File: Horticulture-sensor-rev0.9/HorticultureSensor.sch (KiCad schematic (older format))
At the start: 23 parts, among them J1 Conn_01x04, J2 Conn_02x05_Odd_Even, J3 Conn_01x03, J4 Conn_01x04, J5 Conn_01x03, J6 Conn_01x02, J7 Conn_01x02, J8 Conn_01x01_MountingPin, J9 Conn_01x01_MountingPin, Q1 IRLML2030TRPBF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

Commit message: Initial sensor design
Almost finished, need to work out how power connection should work.
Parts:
- J4: footprint Connector_Molex:Molex_PicoBlade_53398-0371_1x03-1MP_P1.25mm_Vertical -> Connector_Molex:Molex_PicoBlade_53261-0371_1x03-1MP_P1.25mm_Horizontal
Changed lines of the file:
@@
 F 0 "J4" H 11780 6642 50  0000 L CNN
 F 1 "Conn_01x04" H 11780 6551 50  0000 L CNN
-F 2 "Connector_Molex:Molex_PicoBlade_53398-0371_1x03-1MP_P1.25mm_Vertical" H 11700 6650 50  0001 C CNN
+F 2 "Connector_Molex:Molex_PicoBlade_53261-0371_1x03-1MP_P1.25mm_Horizontal" H 11700 6650 50  0001 C CNN
 F 3 "~" H 11700 6650 50  0001 C CNN
 	1    11700 6650

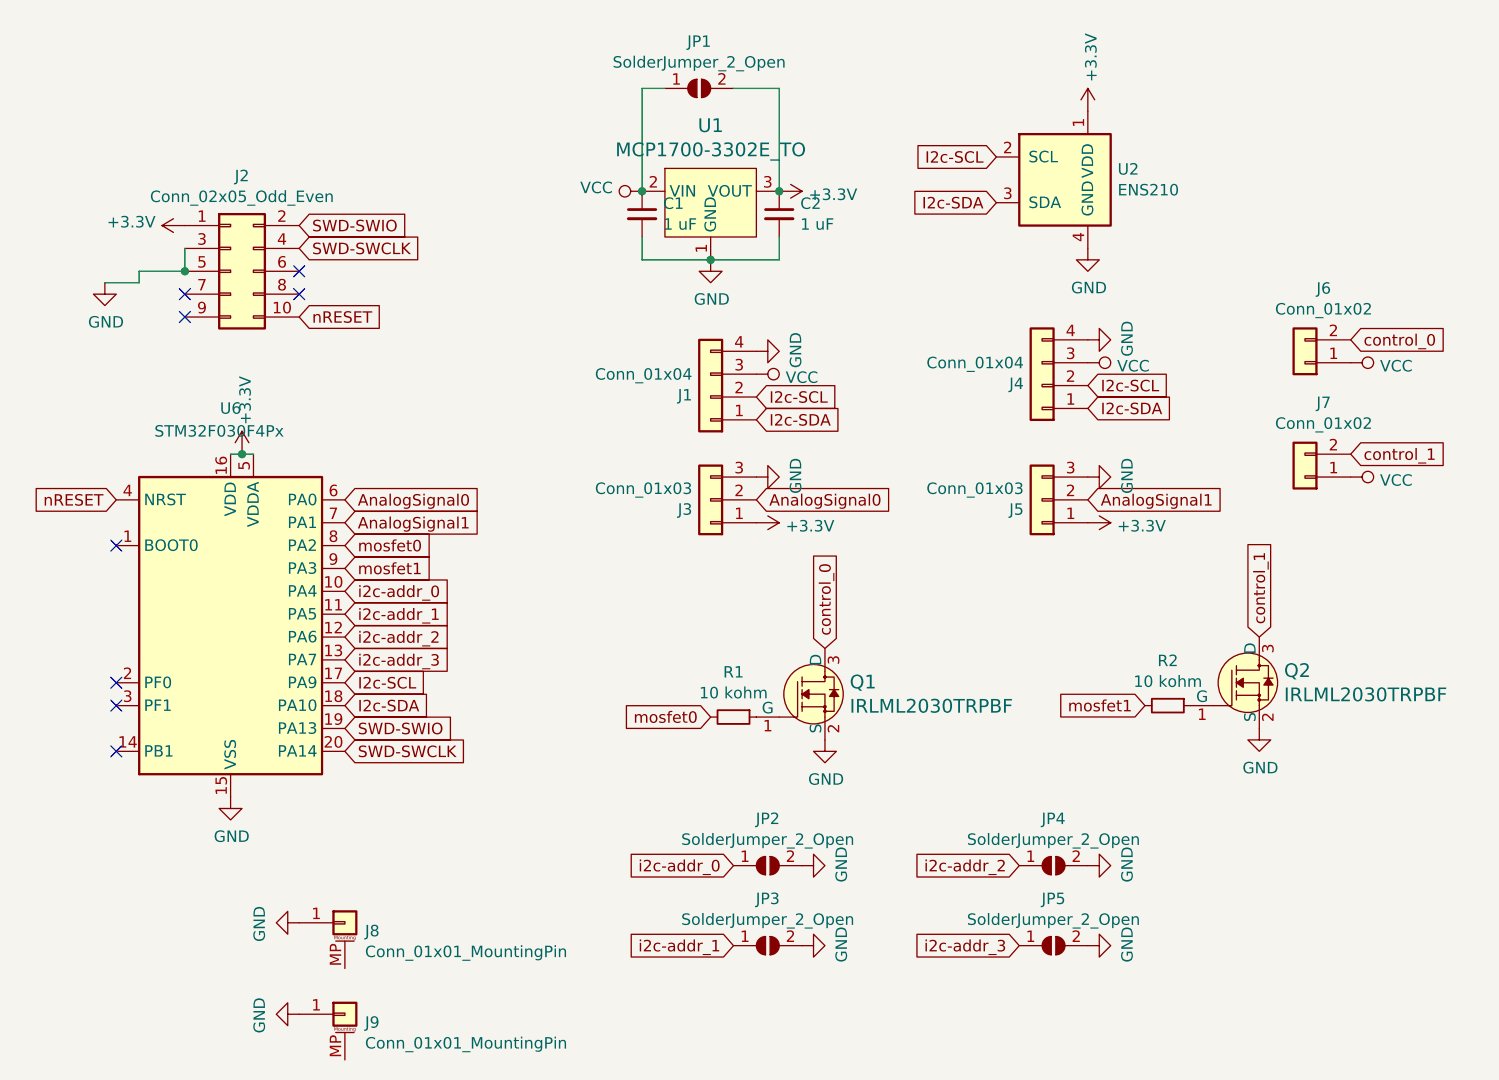
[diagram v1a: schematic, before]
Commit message: Working on sensor board
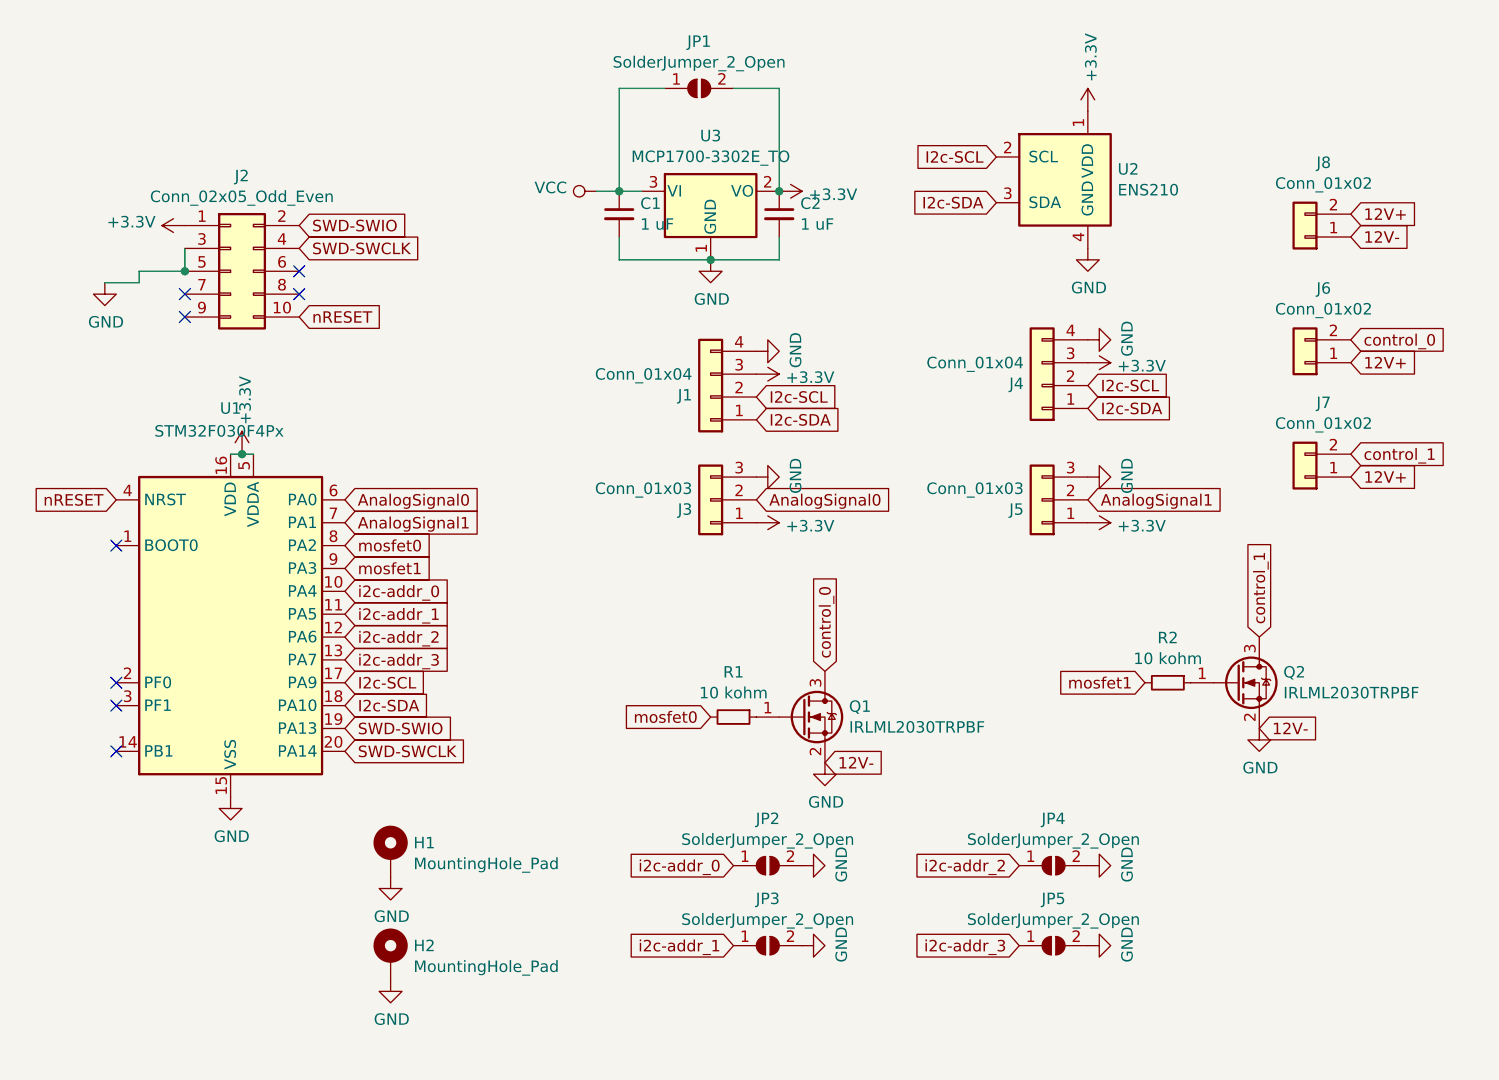
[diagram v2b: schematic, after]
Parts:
- removed J8, J9: Conn_01x01_MountingPin, MountingHole:MountingHole_3.2mm_M3, symbol Connector_Generic_MountingPin:Conn_01x01_MountingPin
- removed Q1, Q2: IRLML2030TRPBF, digikey-footprints:SOT-23-3, symbol dk_Transistors-FETs-MOSFETs-Single:IRLML2402TRPBF
- removed U1: MCP1700-3302E_TO, Package_TO_SOT_SMD:SOT-23, symbol dk_PMIC-Voltage-Regulators-Linear:MCP1700-3302E_TO
- added H1, H2: MountingHole_Pad, MountingHole:MountingHole_3.2mm_M3_Pad, symbol Mechanical:MountingHole_Pad
- added J8: Conn_01x02, Connector_JST:JST_XH_B2B-XH-AM_1x02_P2.50mm_Vertical, symbol Connector_Generic:Conn_01x02
- added Q1, Q2: IRLML2030TRPBF, Package_TO_SOT_SMD:SOT-23, symbol Transistor_FET:IRLML0030
- added U3: MCP1700-3302E_TO, Package_TO_SOT_SMD:SOT-23, symbol Regulator_Linear:MCP1700-1202E_SOT23
- renumbered U6 to U1
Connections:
- net +3V3: now also J1.3 (Pin_3), J4.3 (Pin_3), U3.2 (VO)
- net GND: now also H1.1, H2.1, J8.1 (Pin_1), Q1.2 (S), Q2.2 (S), U3.1 (GND)
- net VCC: now also U3.3 (VI); no longer J1.3 (Pin_3), J4.3 (Pin_3), J6.1 (Pin_1), J7.1 (Pin_1)
- net control_0: now also Q1.3 (D)
- net control_1: now also Q2.3 (D)
- net at R1.1: now also Q1.1 (G)
- net at R2.1: now also Q2.1 (G)
- new net 12V+: J6.1 (Pin_1), J7.1 (Pin_1), J8.2 (Pin_2)
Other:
- moved on the sheet: C1, R2
